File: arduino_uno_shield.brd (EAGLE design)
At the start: 53 x 57.1 mm, 20 parts

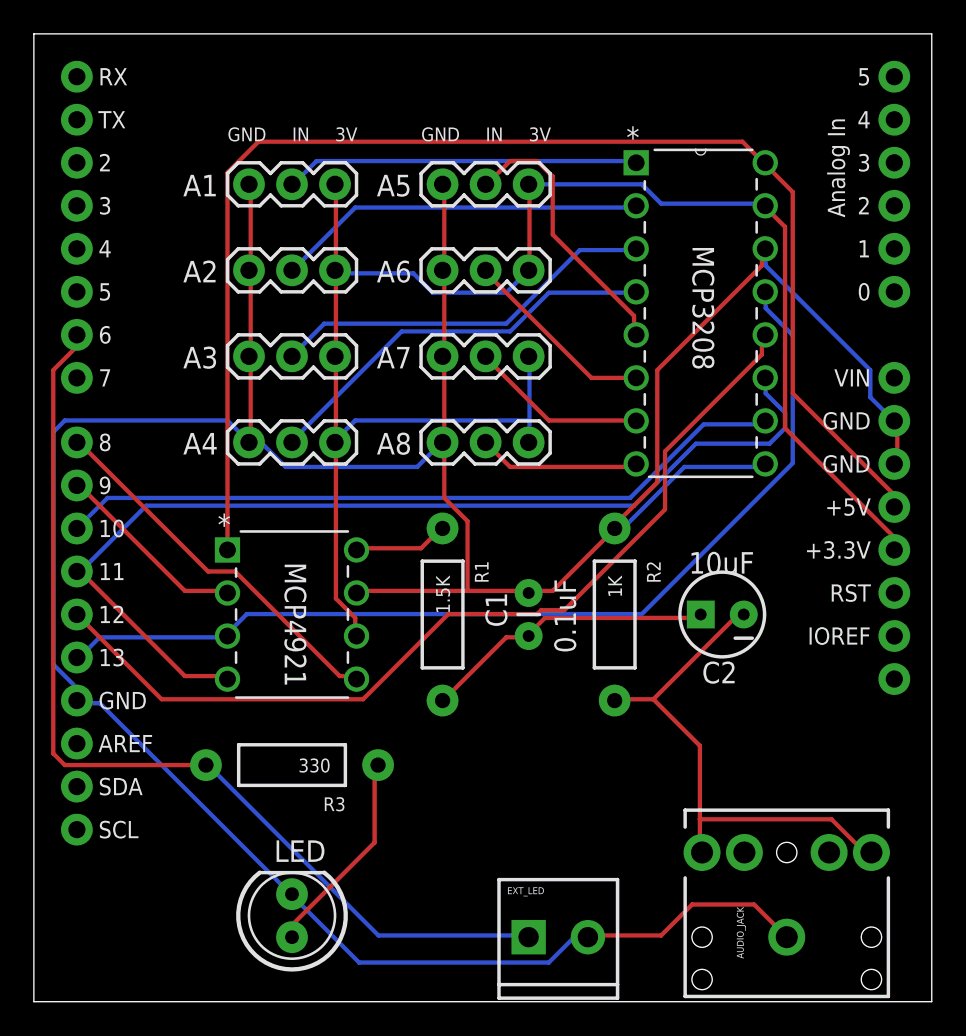
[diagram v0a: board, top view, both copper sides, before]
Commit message: changed layout to reduce interference
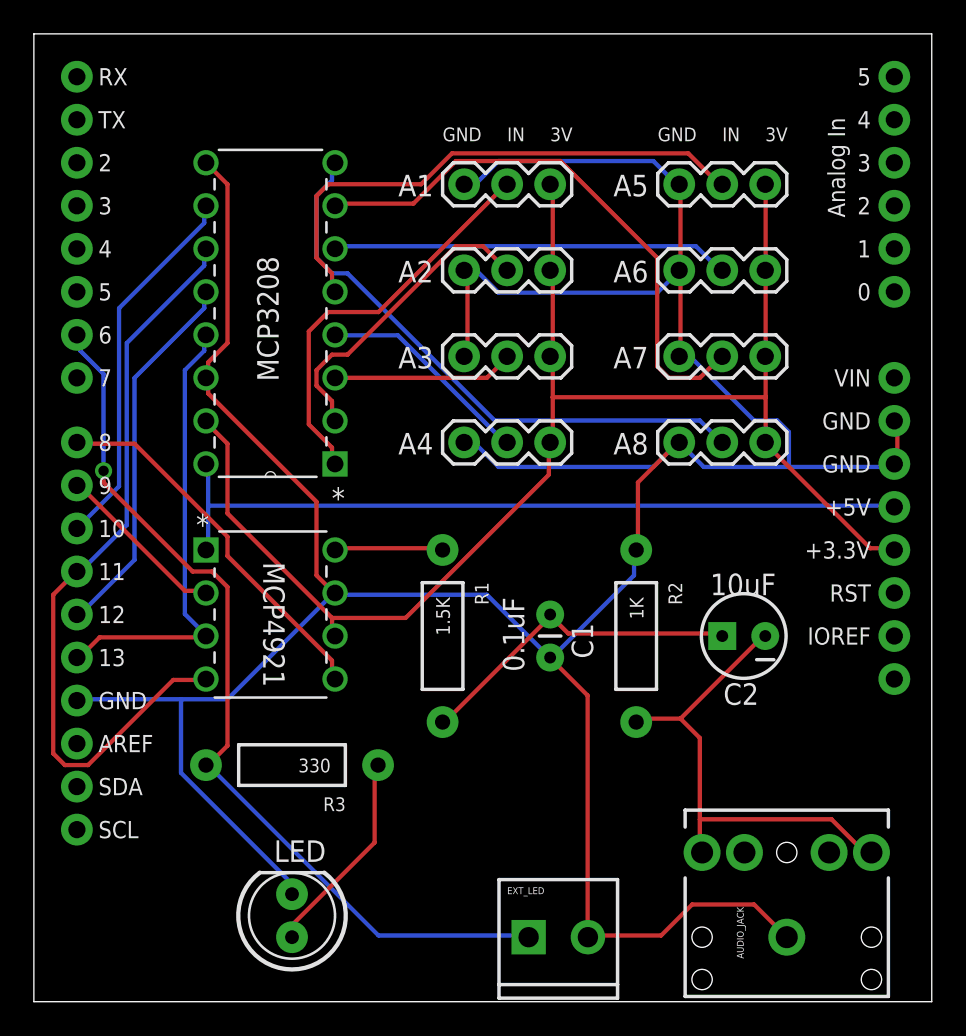
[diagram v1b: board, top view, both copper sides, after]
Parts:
- moved MCP3208 37.5 mm to (10.2, 69.8), turned to 180 degrees
- moved A5 14.0 mm to (38.1, 68.6)
- moved A6 14.0 mm to (38.1, 63.5)
- moved A7 14.0 mm to (38.1, 58.4)
- moved A8 14.0 mm to (38.1, 53.3)
- moved A1 12.7 mm to (25.4, 68.6)
- moved A2 12.7 mm to (25.4, 63.5)
- moved A3 12.7 mm to (25.4, 58.4)
- moved A4 12.7 mm to (25.4, 53.3)
- moved R2 1.80 mm to (35.6, 41.9)
- moved C1 1.80 mm to (30.5, 43.2), turned to 270 degrees
- moved C2 1.80 mm to (41.9, 41.9)
- moved R1 1.27 mm to (24.1, 41.9)
- moved MCP4921 1.27 mm to (17.8, 39.4)
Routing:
- net 5V: track 78.7 -> 45.7 mm
- net SPI_MISO: track 54.3 -> 22.3 mm
- net SPI_CLK: track 57.9 -> 27.0 mm
- net N$18: track 9.58 -> 34.5 mm
- net N$17: track 10.5 -> 33.6 mm
- net CS_ADC: track 43.3 -> 22.2 mm
- net N$1: track 16.3 -> 31.9 mm
- net SPI_MOSI: track 60.4 -> 45.1 mm
- net N$14: track 22.9 -> 10.7 mm
- net 3.3V: track 100.1 -> 88.0 mm
- net N$16: track 11.6 -> 23.5 mm
- net N$15: track 24.0 -> 12.9 mm
- net GND: track 196.3 -> 206.4 mm
- net N$12: track 57.8 -> 53.7 mm, vias 0 -> 1
- net N$2: track 21.9 -> 18.4 mm
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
